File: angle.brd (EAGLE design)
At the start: 58 x 29.8 mm, 12 parts

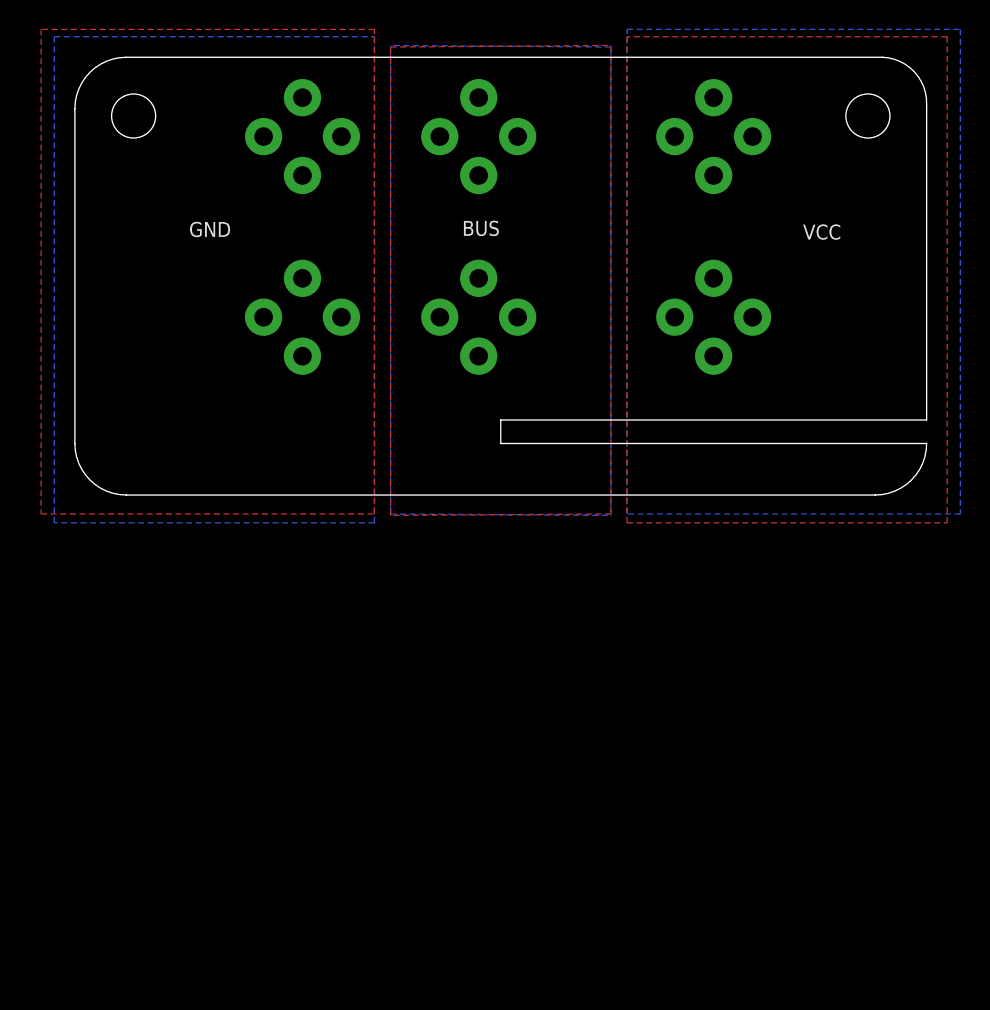
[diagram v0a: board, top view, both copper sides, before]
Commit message: doubled and mirrored angle pcb
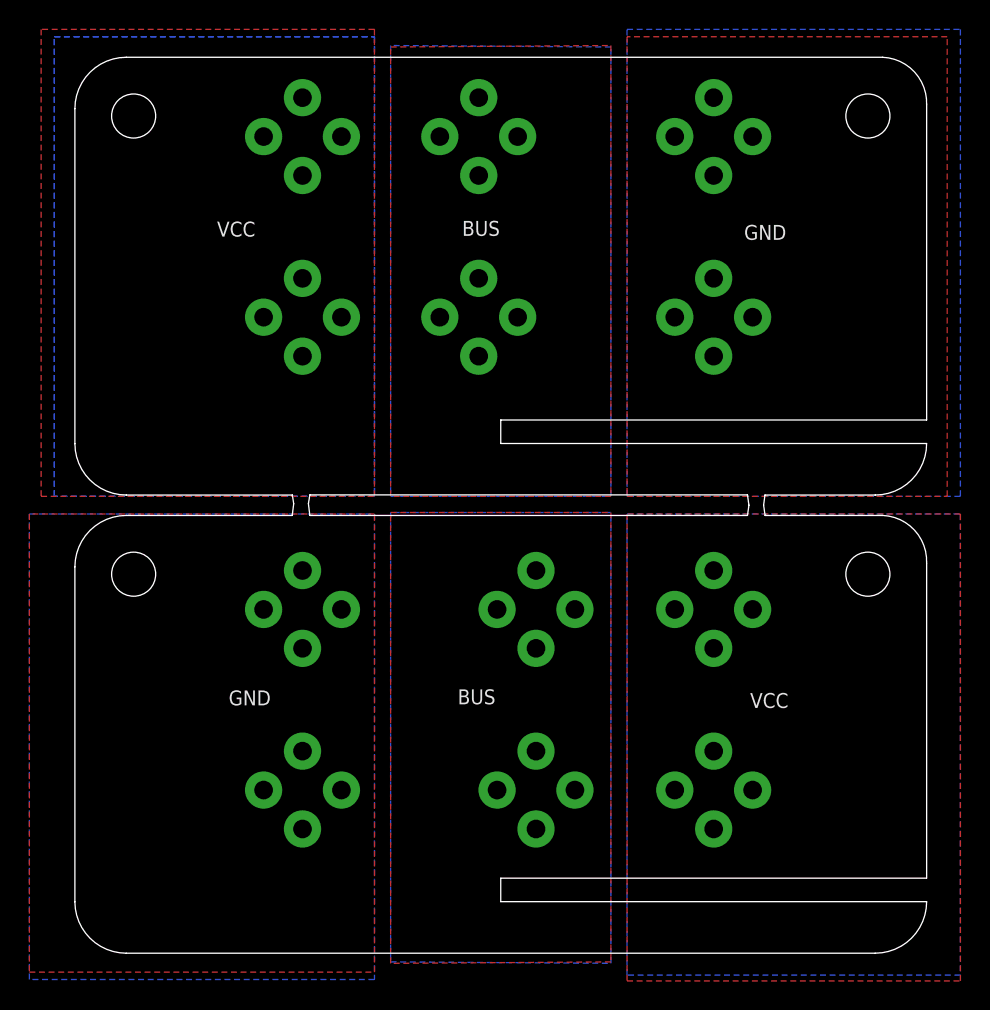
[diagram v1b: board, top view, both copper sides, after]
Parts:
- removed GND-CLIP1, GND-CLIP2, PWM-CLIP2, PWM-CLIP3: FUSE-HOLDER-5X20MM, timon-diverses:FUSE-HOLDER-5X20MM
- added ABUS-CLIP2, ABUS-CLIP3, AGND-CLIP1, AGND-CLIP2, BBUS-CLIP, BBUS-CLIP1, BBUS-CLIP2, BBUS-CLIP3, BGND-CLIP, BGND-CLIP1, BGND-CLIP2, BGND-CLIP3, BVCC-CLIP, BVCC-CLIP1, BVCC-CLIP2, BVCC-CLIP3: FUSE-HOLDER-5X20MM, timon-diverses:FUSE-HOLDER-5X20MM
- renumbered GND-CLIP to AGND-CLIP, GND-CLIP3 to AGND-CLIP3, PWM-CLIP to ABUS-CLIP, PWM-CLIP1 to ABUS-CLIP1, VCC-CLIP to AVCC-CLIP, VCC-CLIP1 to AVCC-CLIP1, VCC-CLIP2 to AVCC-CLIP2, VCC-CLIP3 to AVCC-CLIP3
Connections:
- net VCC-RAW renamed AVCC-RAW
- removed net GND: AGND-CLIP.CLIP-INPUT1, AGND-CLIP.CLIP-INPUT2, AGND-CLIP3.CLIP-INPUT1, AGND-CLIP3.CLIP-INPUT2, GND-CLIP1.CLIP-INPUT1, GND-CLIP1.CLIP-INPUT2, GND-CLIP2.CLIP-INPUT1, GND-CLIP2.CLIP-INPUT2
- removed net PWM: ABUS-CLIP.CLIP-INPUT1, ABUS-CLIP.CLIP-INPUT2, ABUS-CLIP1.CLIP-INPUT1, ABUS-CLIP1.CLIP-INPUT2, PWM-CLIP2.CLIP-INPUT1, PWM-CLIP2.CLIP-INPUT2, PWM-CLIP3.CLIP-INPUT1, PWM-CLIP3.CLIP-INPUT2
- new net ABUS: ABUS-CLIP.CLIP-INPUT1, ABUS-CLIP.CLIP-INPUT2, ABUS-CLIP1.CLIP-INPUT1, ABUS-CLIP1.CLIP-INPUT2, ABUS-CLIP2.CLIP-INPUT1, ABUS-CLIP2.CLIP-INPUT2, ABUS-CLIP3.CLIP-INPUT1, ABUS-CLIP3.CLIP-INPUT2
- new net AGND: AGND-CLIP.CLIP-INPUT1, AGND-CLIP.CLIP-INPUT2, AGND-CLIP1.CLIP-INPUT1, AGND-CLIP1.CLIP-INPUT2, AGND-CLIP2.CLIP-INPUT1, AGND-CLIP2.CLIP-INPUT2, AGND-CLIP3.CLIP-INPUT1, AGND-CLIP3.CLIP-INPUT2
- new net BBUS: BBUS-CLIP.CLIP-INPUT1, BBUS-CLIP.CLIP-INPUT2, BBUS-CLIP1.CLIP-INPUT1, BBUS-CLIP1.CLIP-INPUT2, BBUS-CLIP2.CLIP-INPUT1, BBUS-CLIP2.CLIP-INPUT2, BBUS-CLIP3.CLIP-INPUT1, BBUS-CLIP3.CLIP-INPUT2
- new net BGND: BGND-CLIP.CLIP-INPUT1, BGND-CLIP.CLIP-INPUT2, BGND-CLIP1.CLIP-INPUT1, BGND-CLIP1.CLIP-INPUT2, BGND-CLIP2.CLIP-INPUT1, BGND-CLIP2.CLIP-INPUT2, BGND-CLIP3.CLIP-INPUT1, BGND-CLIP3.CLIP-INPUT2
- new net BVCC-RAW: BVCC-CLIP.CLIP-INPUT1, BVCC-CLIP.CLIP-INPUT2, BVCC-CLIP1.CLIP-INPUT1, BVCC-CLIP1.CLIP-INPUT2, BVCC-CLIP2.CLIP-INPUT1, BVCC-CLIP2.CLIP-INPUT2, BVCC-CLIP3.CLIP-INPUT1, BVCC-CLIP3.CLIP-INPUT2
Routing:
- added copper zone on layer 1, net ABUS
- added copper zone on layer 16, net ABUS
- added copper zone on layer 1, net AGND
- added copper zone on layer 16, net AGND
- added copper zone on layer 1, net BBUS
- added copper zone on layer 16, net BBUS
- added copper zone on layer 1, net BGND
- added copper zone on layer 16, net BGND
- added copper zone on layer 1, net BVCC-RAW
- added copper zone on layer 16, net BVCC-RAW
- removed copper zone on layer 1, net GND
- removed copper zone on layer 16, net GND
- removed copper zone on layer 1, net PWM
- removed copper zone on layer 16, net PWM
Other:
- board size 58 x 29.8 mm -> 58 x 61 mm
